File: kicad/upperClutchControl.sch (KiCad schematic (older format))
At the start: 12 parts

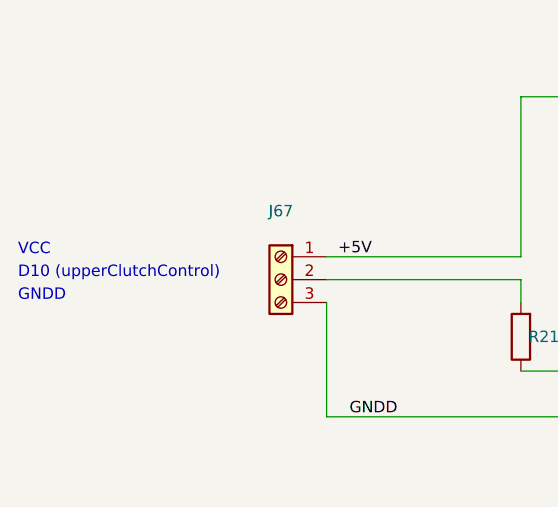
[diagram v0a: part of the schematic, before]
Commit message: KICAD: Actualizar pines de control en .sch de embragues y freno
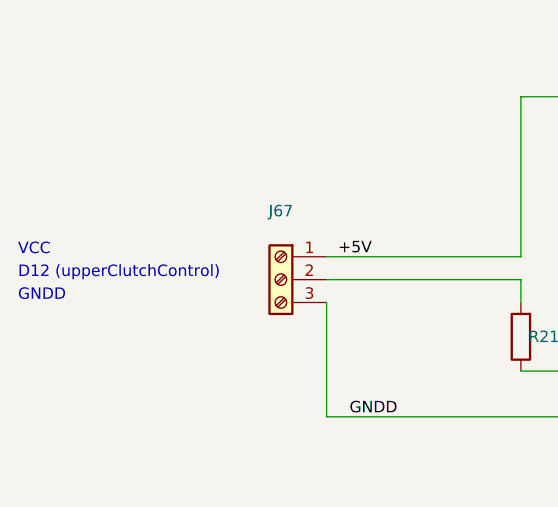
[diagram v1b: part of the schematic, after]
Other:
- note added: "D12 (upperClutchControl)"
- note removed: "D10 (upperClutchControl)"
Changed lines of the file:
@@
 Sheet 16 22
 Title "Mainet-mega -- upperClutchControl"
-Date "2021-07-20"
+Date "2021-07-29"
 Rev "1.0"
 Comp "Tovenca"
@@
 upperClutchControl
 Text Notes 2850 3800 0    50   ~ 0
-D10 (upperClutchControl)
+D12 (upperClutchControl)
 Text Notes 2850 3900 0    50   ~ 0
 GNDD
